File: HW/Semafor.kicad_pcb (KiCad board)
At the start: 2 copper layers, 200.8 x 212.8 mm, 93 parts, among them J1 USB_C_Receptacle_USB2.0, J2 USB_plug, M1 Motor_DC, Q1 Q_NMOS_GSD, Q2 Q_NMOS_GSD, Q3 Q_NMOS_GSD, Q4 Q_NMOS_GSD, SW6 SW_SPDT, U1 ESP32-C3, U2 CN3058E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

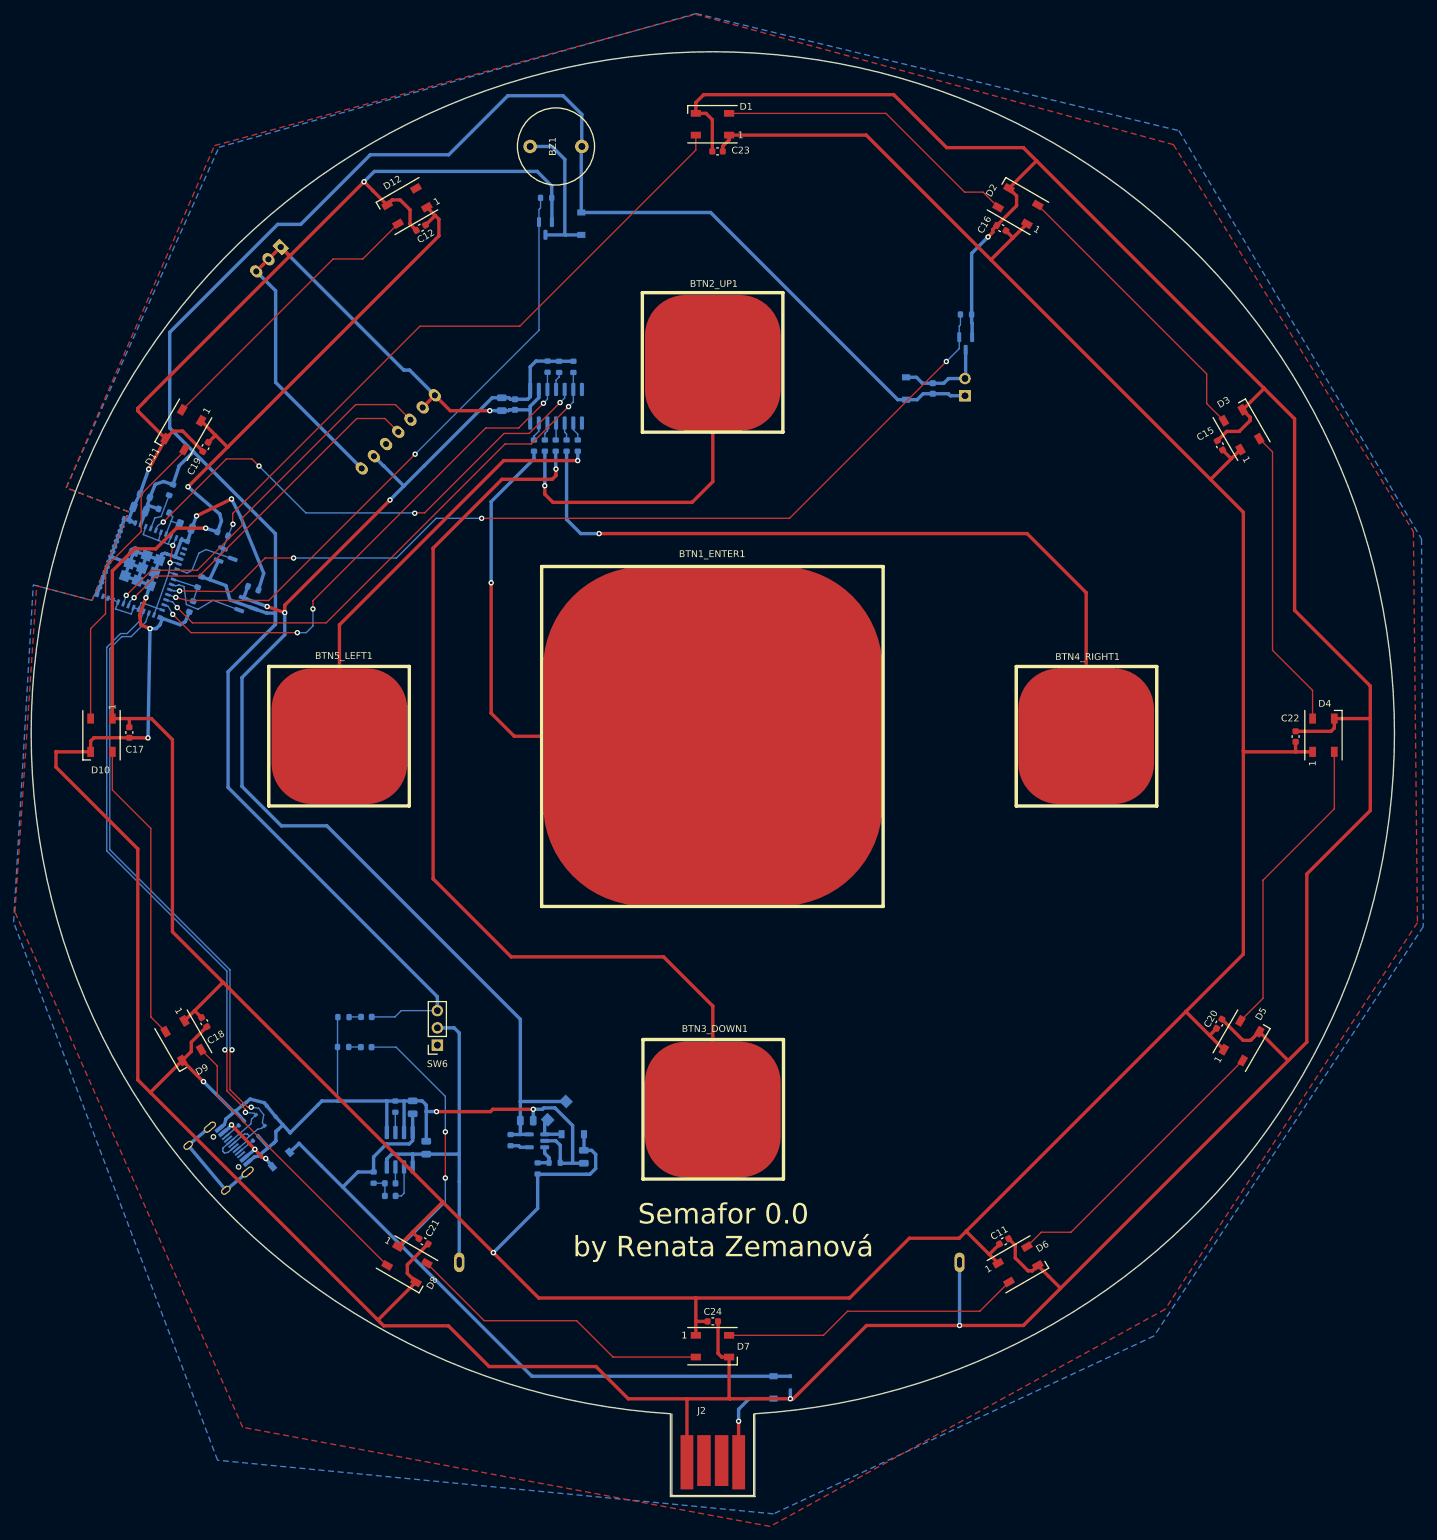
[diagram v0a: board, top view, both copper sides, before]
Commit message: reduction dimensions of PCB + routing, update fabrication files
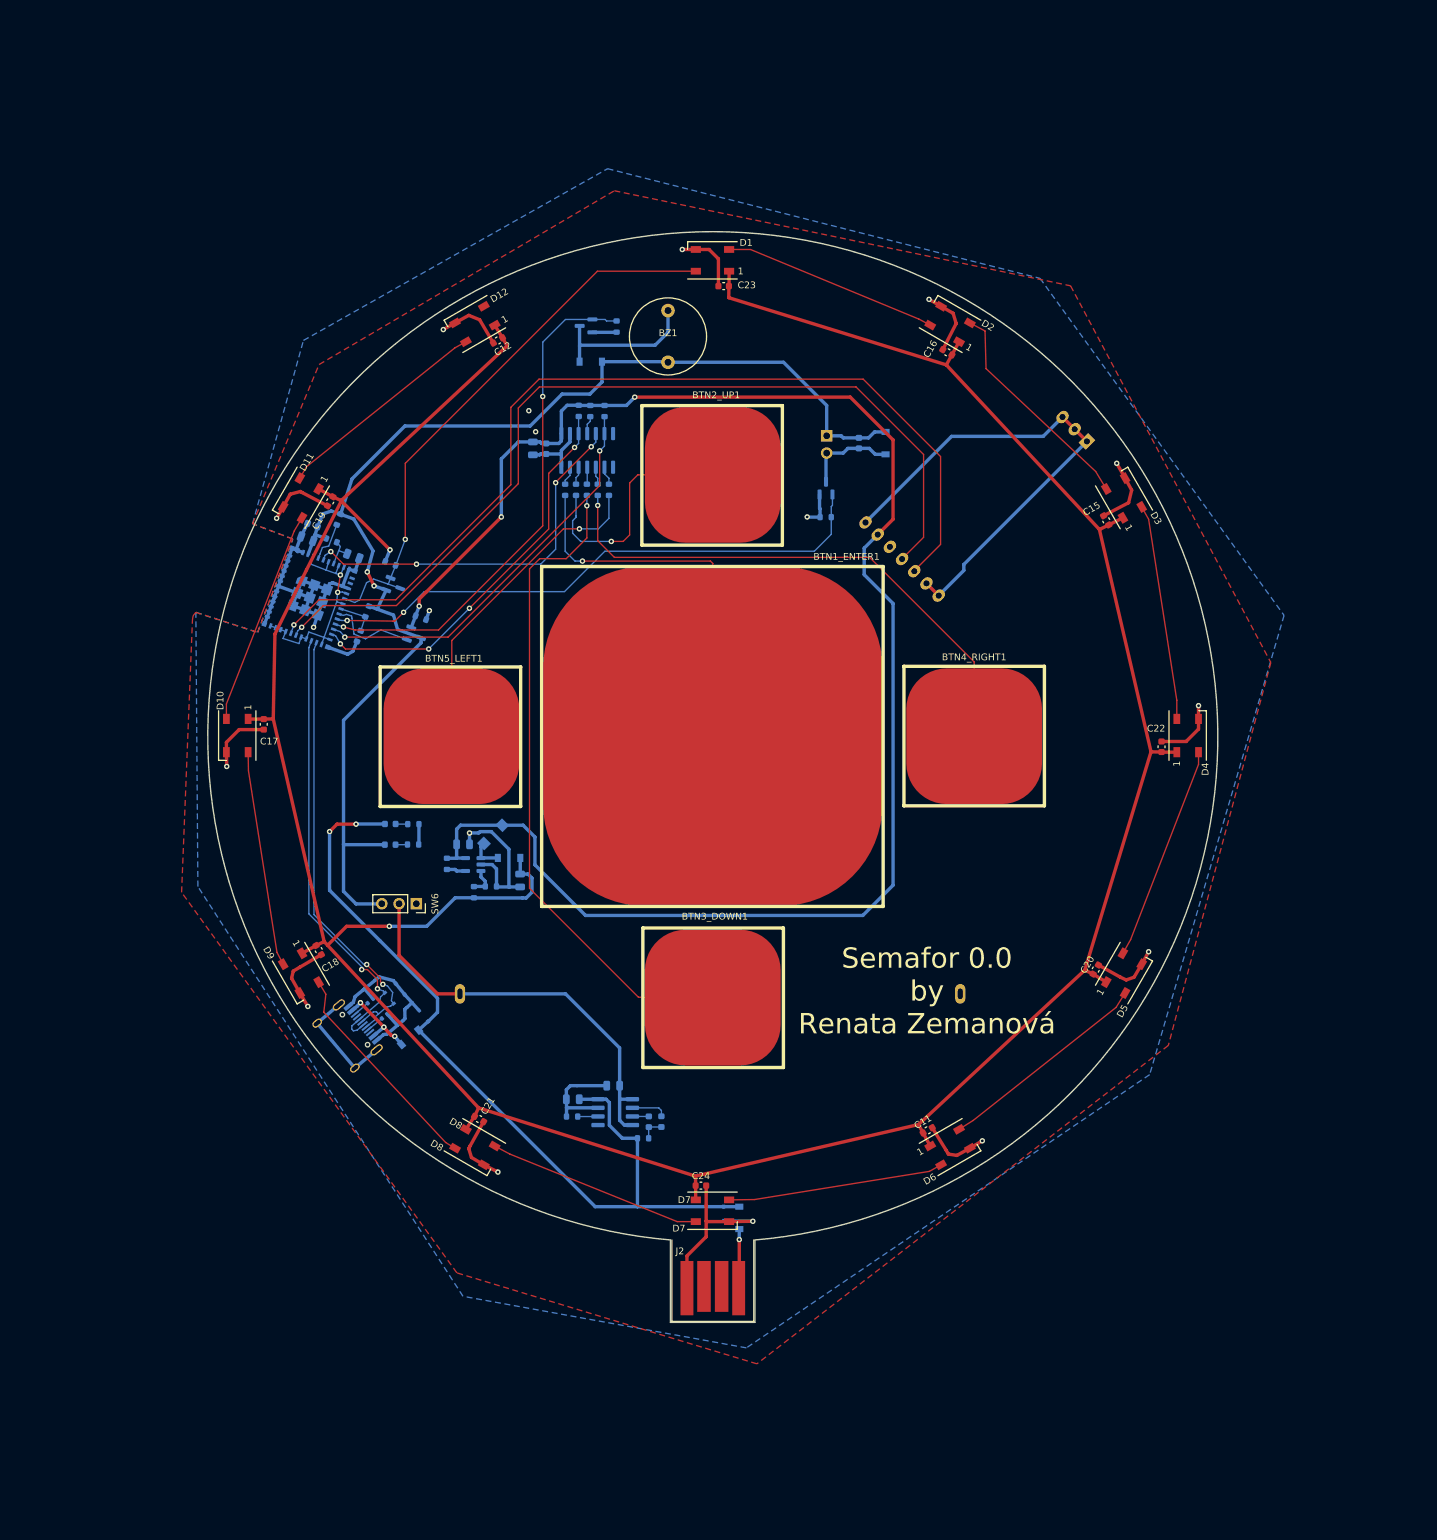
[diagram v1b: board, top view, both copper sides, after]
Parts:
- moved U4 99.3 mm to (-60.5, -137.8), turned to -45 degrees
- moved C13 41.8 mm to (-136.8, -84.1)
- moved C14 41.8 mm to (-128.4, -78.8)
- moved D17 41.8 mm to (-130.0, -82.1)
- moved R10 41.8 mm to (-132.7, -77.9)
- moved R13 41.8 mm to (-139.2, -81.2)
- moved R9 41.8 mm to (-135.2, -77.0)
- moved L1 41.8 mm to (-132.4, -85.5)
- moved U3 41.8 mm to (-135.3, -81.1)
- moved D13 41.4 mm to (-107.6, -43.2), turned to -90 degrees
- moved R6 40.1 mm to (-110.3, -40.8), turned to 0 degrees
- moved BT1 39.6 mm to (-99.9, -62.1)
- moved D14 39.2 mm to (-109.4, -43.2), turned to -90 degrees
- moved R15 36.3 mm to (-83.4, -132.3), turned to 180 degrees
- moved R11 34.4 mm to (-144.1, -87.0), turned to 0 degrees
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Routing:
- net GND: track 1089.1 -> 361.1 mm, vias 14 -> 18
- net PWR_LED: track 626.8 -> 466.1 mm, vias 3 -> 2
- net +3V3: track 325.8 -> 193.8 mm, vias 0 -> 2
- net RX_LoRa: track 56.4 -> 141.5 mm
- net TX_LoRa: track 52.1 -> 135.1 mm
- net 3V3_SWITCHED: track 185.6 -> 247.3 mm
- net MOTOR: track 136.3 -> 84.0 mm, vias 4 -> 2
- net Net-(BTN3_DOWN1-Pad1): track 139.1 -> 97.3 mm
- net Net-(BTN4_RIGHT1-Pad1): track 112.2 -> 80.5 mm
- net D-: track 97.9 -> 67.4 mm
- net D+: track 96.6 -> 67.0 mm
- net DATA_LED: track 109.5 -> 83.2 mm
- net CHANGE_OF_CAP_BUT: track 76.3 -> 56.0 mm
- net SDA: track 78.7 -> 58.7 mm
- net SCL: track 79.2 -> 59.3 mm
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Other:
- board size 200.8 x 212.8 mm -> 148.8 x 160.7 mm

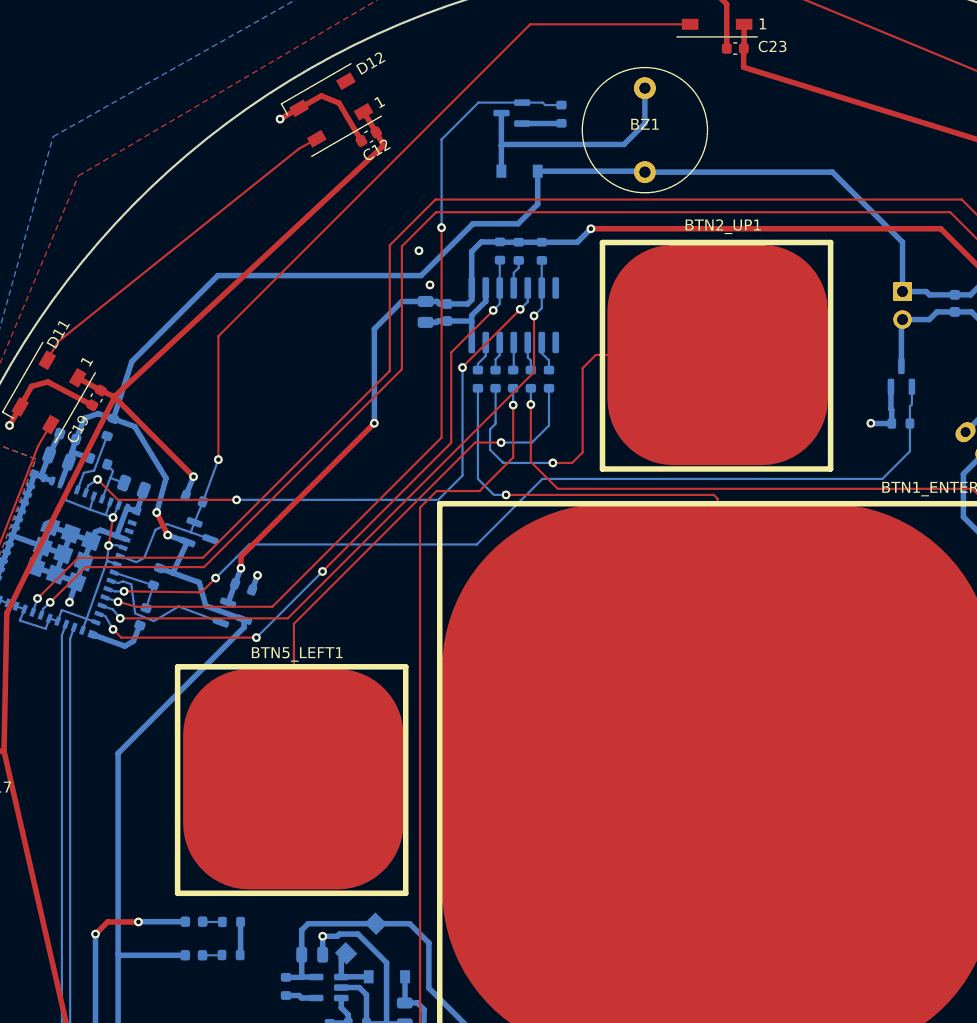
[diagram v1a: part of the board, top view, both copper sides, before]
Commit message: repair mistakes from prototype PCB
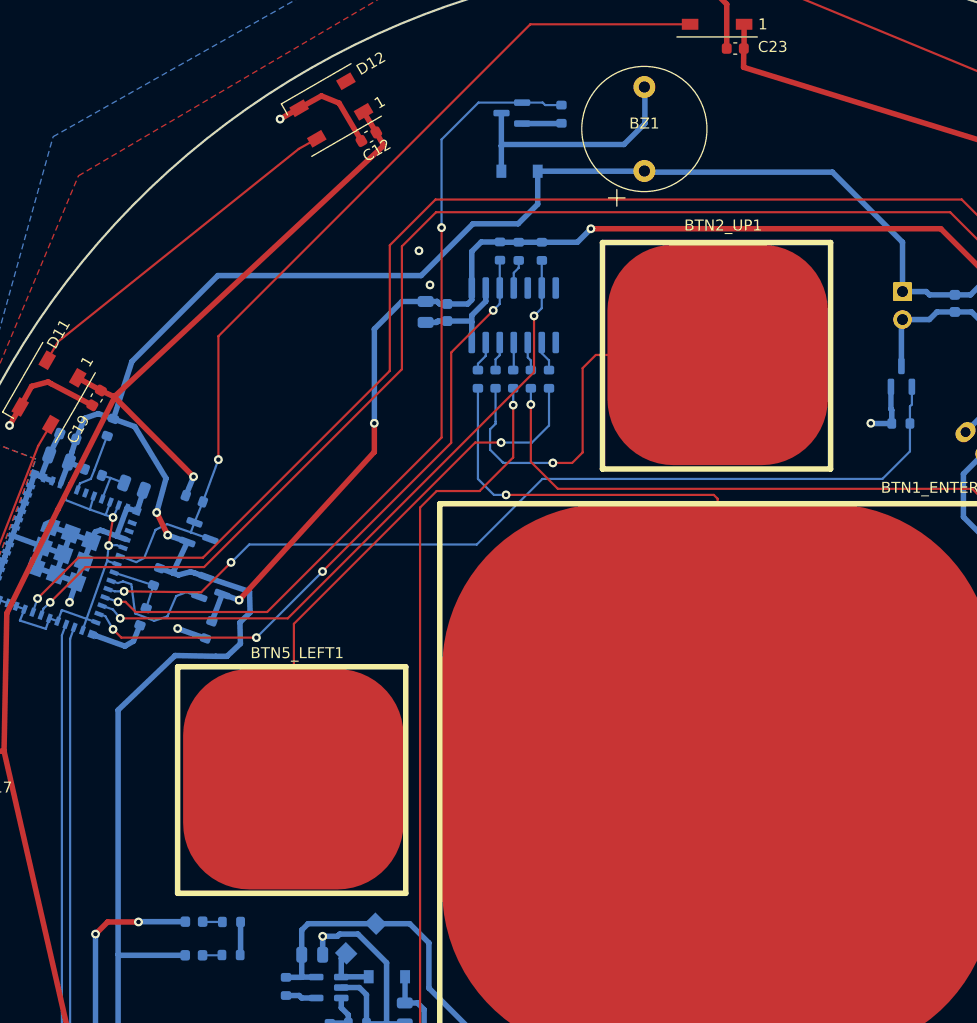
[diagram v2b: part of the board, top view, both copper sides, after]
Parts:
- Q2: value Q_NMOS_GSD -> Q_PMOS_GSD
- moved R25 5.02 mm to (-146.2, -113.5), turned to -110 degrees
- moved Q2 3.05 mm to (-145.8, -117.1)
- moved R5 1.11 mm to (-156.7, -127.8)
- moved BZ1 0.12 mm to (-106.7, -159.0)
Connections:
- Q2 pad 2: 3V3_SWITCHED -> +3V3
- Q2 pad 3: +3V3 -> 3V3_SWITCHED
- U1 pad 6: CHANGE_OF_CAP_BUT -> unconnected-(U1-Pad6)
- U5 pad 5: CHANGE_OF_CAP_BUT -> unconnected-(U5-Pad5)
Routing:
- net CHANGE_OF_CAP_BUT: track 56.0 -> 0.00 mm, vias 4 -> 0
- net +3V3: track 193.8 -> 198.2 mm
- net 3V3_SWITCHED: track 247.3 -> 250.9 mm
- net GND: track 361.1 -> 362.3 mm
- net Net-(U1-Pad19): track 13.2 -> 12.0 mm
- net Net-(C2-Pad1): track 4.86 -> 4.20 mm
- net PIEZO: track 76.4 -> 76.9 mm

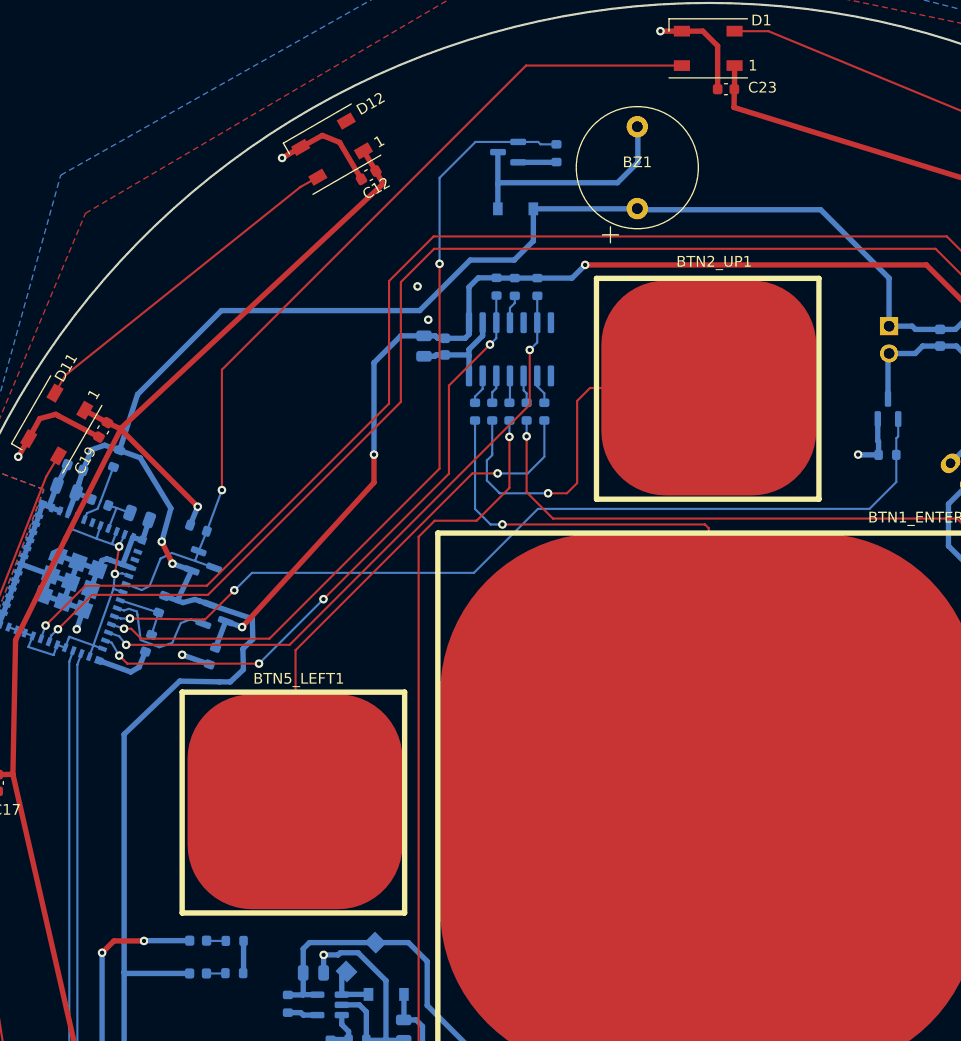
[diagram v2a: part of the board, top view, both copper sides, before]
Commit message: add phototransistor and connector for programmable LEDs (on side)
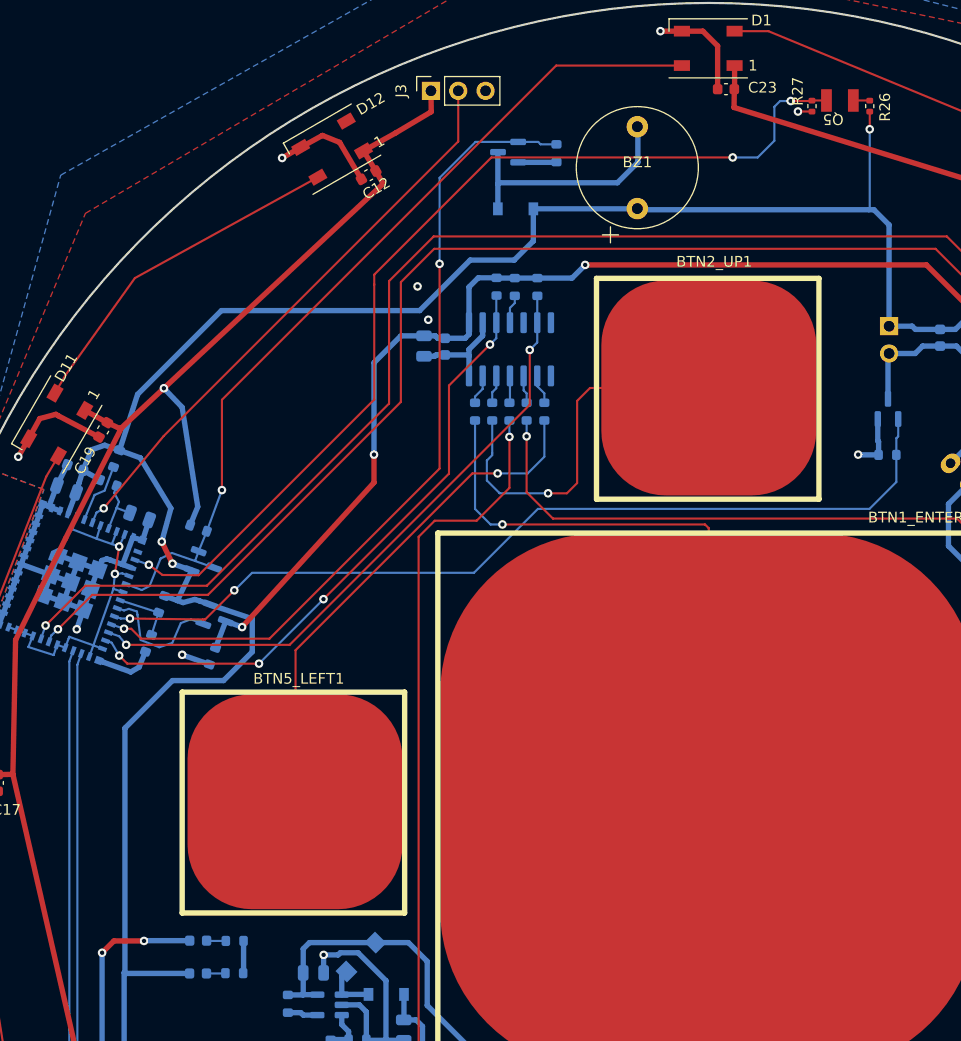
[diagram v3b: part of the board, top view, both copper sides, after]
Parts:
- added J3: Conn_01x03_Male, Connector_PinSocket_2.54mm:PinSocket_1x03_P2.54mm_Vertical, F.Cu at (-125.8, -166.2)
- added Q5: Q_Photo_NPN, Library:SMD,3.5x2.8x1.9mm, F.Cu at (-88.0, -165.2)
- added R26: 22k, Resistor_SMD:R_0402_1005Metric, F.Cu at (-85.0, -164.7)
- added R27: 10k, Resistor_SMD:R_0402_1005Metric, F.Cu at (-90.4, -164.7)
- moved R5 1.98 mm to (-155.9, -129.7)
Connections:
- U1 pad 13: unconnected-(U1-Pad13) -> FOTOTRANZISTOR
- U1 pad 6: unconnected-(U1-Pad6) -> DATA_LED_SIDE
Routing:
- net FOTOTRANZISTOR: track 0.00 -> 91.7 mm, vias 0 -> 3
- net DATA_LED_SIDE: track 0.00 -> 54.0 mm, vias 0 -> 1
- net +3V3: track 198.2 -> 210.4 mm, vias 2 -> 3
- net PWR_LED: track 466.1 -> 476.9 mm
- net DATA_LED: track 83.2 -> 81.6 mm
- net Net-(Q5-Pad1): track 0.00 -> 1.53 mm
- net Net-(C2-Pad1): track 4.20 -> 5.63 mm
- net GND: track 362.3 -> 363.6 mm, vias 18 -> 19
- net Net-(D11-Pad2): track 31.8 -> 32.5 mm
